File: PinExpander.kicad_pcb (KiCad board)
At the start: 2 copper layers, 73 x 33 mm, 35 parts, among them J1 CONN_01X08, J2 CONN_01X08, J3 CONN_01X08, J4 CONN_01X05, U1 74HC595, U2 74HC595, U3 74HC595

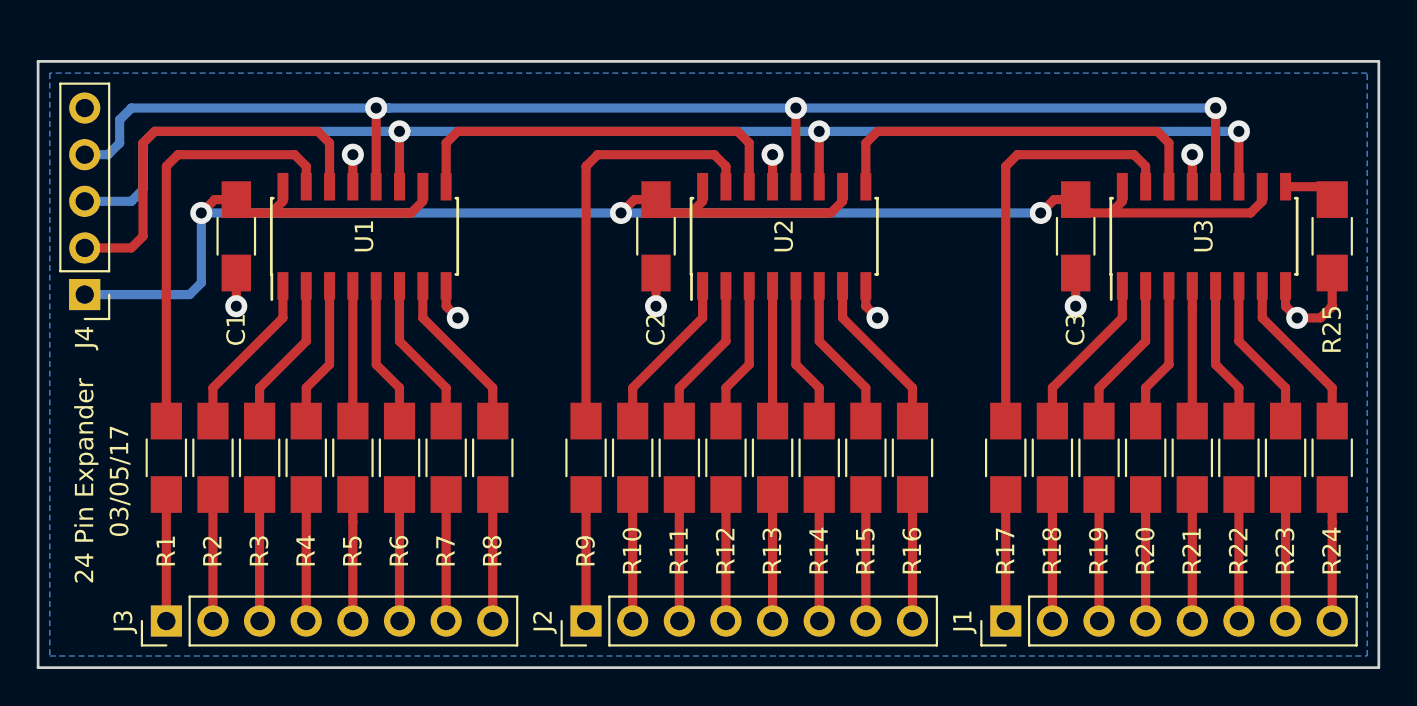
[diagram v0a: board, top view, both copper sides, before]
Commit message: New stackable version
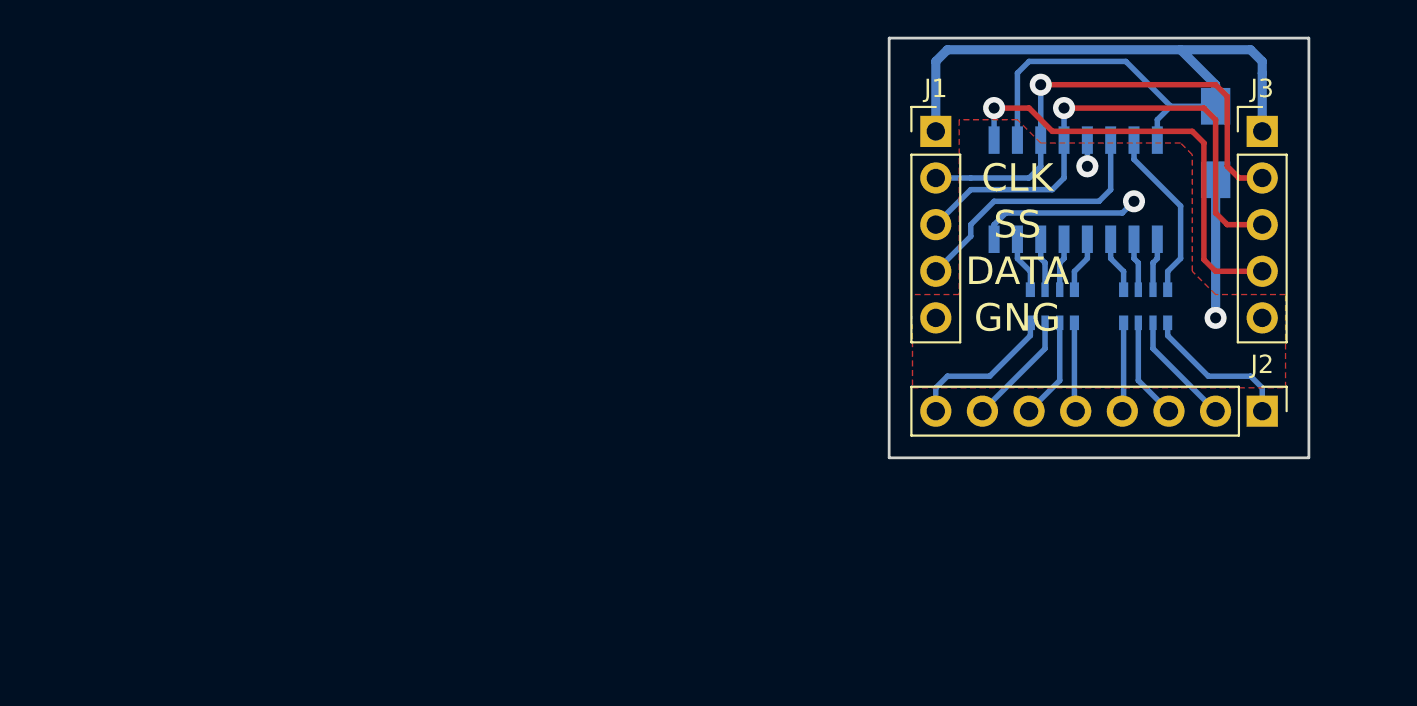
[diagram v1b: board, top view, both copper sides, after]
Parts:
- removed C2, C3: 100n, Capacitors_SMD:C_1206_HandSoldering
- removed J4: CONN_01X05, Pin_Headers:Pin_Header_Straight_1x05_Pitch2.54mm
- removed R1, R10, R11, R12, R13, R14, R15, R16, R17, R18, R19, R2, R20, R21, R22, R23, R24, R3, R4, R5, R6, R7, R8, R9: 560R, Resistors_SMD:R_1206_HandSoldering
- removed R25: 10K, Resistors_SMD:R_1206_HandSoldering
- removed U2, U3: 74HC595, Housings_SOIC:SOIC-16_3.9x9.9mm_Pitch1.27mm
- added RN1: R_Pack04, Resistors_SMD:R_Array_Convex_4x0603, B.Cu at (167.6, 78.1)
- added RN2: R_Pack04, Resistors_SMD:R_Array_Convex_4x0603, B.Cu at (162.6, 78.1)
- C1, U1: moved to B.Cu
- J1, J3: value CONN_01X08 -> CONN_01X05; footprint Pin_Headers:Pin_Header_Straight_1x08_Pitch2.54mm -> Pin_Headers:Pin_Header_Straight_1x05_Pitch2.54mm
- moved J3 65.4 mm to (174.0, 68.6), turned to 0 degrees
- moved C1 53.6 mm to (171.4, 69.2)
- moved U1 38.8 mm to (163.8, 71.8)
- moved J2 38.6 mm to (174.0, 83.8), turned to 270 degrees
- moved J1 26.9 mm to (156.2, 68.6), turned to 0 degrees
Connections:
- J1 pad 1: Net-(J1-Pad1) -> VCC
- J1 pad 2: Net-(J1-Pad2) -> /CLOCK
- J1 pad 3: Net-(J1-Pad3) -> /SS
- J1 pad 4: Net-(J1-Pad4) -> /DATA
- J1 pad 5: Net-(J1-Pad5) -> GND
- J3 pad 1: Net-(J3-Pad1) -> VCC
- J3 pad 2: Net-(J3-Pad2) -> /CLOCK
- J3 pad 3: Net-(J3-Pad3) -> /SS
- J3 pad 5: Net-(J3-Pad5) -> GND
- U1 pad 12: /OutputLoad -> /SS
- U1 pad 14: /MOSI -> /DATA
- U1 pad 9: Net-(U1-Pad9) -> Net-(J3-Pad4)
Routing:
- net /OutputLoad: track 76.2 -> 0.00 mm, vias 3 -> 0
- net VCC: track 102.4 -> 47.7 mm, vias 3 -> 0
- net /CLOCK: track 75.0 -> 26.8 mm, vias 3 -> 1
- net /SS: track 0.00 -> 28.2 mm, vias 0 -> 1
- net Net-(R9-Pad2): track 23.1 -> 0.00 mm
- net Net-(R17-Pad2): track 23.1 -> 0.00 mm
- net Net-(U1-Pad9): track 21.8 -> 0.00 mm
- net Net-(U2-Pad9): track 21.8 -> 0.00 mm
- net /MOSI: track 21.6 -> 0.00 mm
- net Net-(J3-Pad4): track 6.89 -> 23.8 mm, vias 0 -> 1
- net /DATA: track 0.00 -> 14.4 mm
- net Net-(RN1-Pad8): track 23.1 -> 9.49 mm
- net Net-(R24-Pad2): track 8.94 -> 0.00 mm
- net Net-(R18-Pad2): track 8.94 -> 0.00 mm
- net Net-(R16-Pad2): track 8.94 -> 0.00 mm
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- added copper zone on F.Cu, net GND
- removed copper zone on B.Cu, net GND
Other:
- board size 73 x 33 mm -> 22.9 x 22.9 mm
- net class Default: clearance 0.4 -> 0.3; trace_width 0.5 -> 0.3
- rule trace_clearance: 0.4 -> 0.3
- board text added: "CLK"
- board text added: "DATA"
- board text added: "GNG"
- board text added: "SS"
- board text removed: "00"
- board text removed: "01"
- board text removed: "02"
- board text removed: "03"
- board text removed: "03/05/17"
- board text removed: "04"
- board text removed: "05"
- board text removed: "06"
- board text removed: "07"
- board text removed: "08"
- board text removed: "09"
- board text removed: "10"
- board text removed: "11"
- board text removed: "12"
- board text removed: "13"
- board text removed: "14"
- board text removed: "15"
- board text removed: "16"
- board text removed: "17"
- board text removed: "18"
- board text removed: "19"
- board text removed: "20"
- board text removed: "21"
- board text removed: "22"
- board text removed: "23"
- board text removed: "24 Pin Expander"
